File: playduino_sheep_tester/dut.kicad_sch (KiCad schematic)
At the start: 48 parts, among them J2 Conn_02x14_Odd_Even, J3 Conn_01x04_Pin, K2 G6K-2F-Y-TR DC5, K3 G6K-2F-Y-TR DC5, K4 G6K-2F-Y-TR DC5, K5 G6K-2F-Y-TR DC5, K6 G6K-2F-Y-TR DC5, Q11 AO3416, Q12 AO3416, Q13 AO3416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

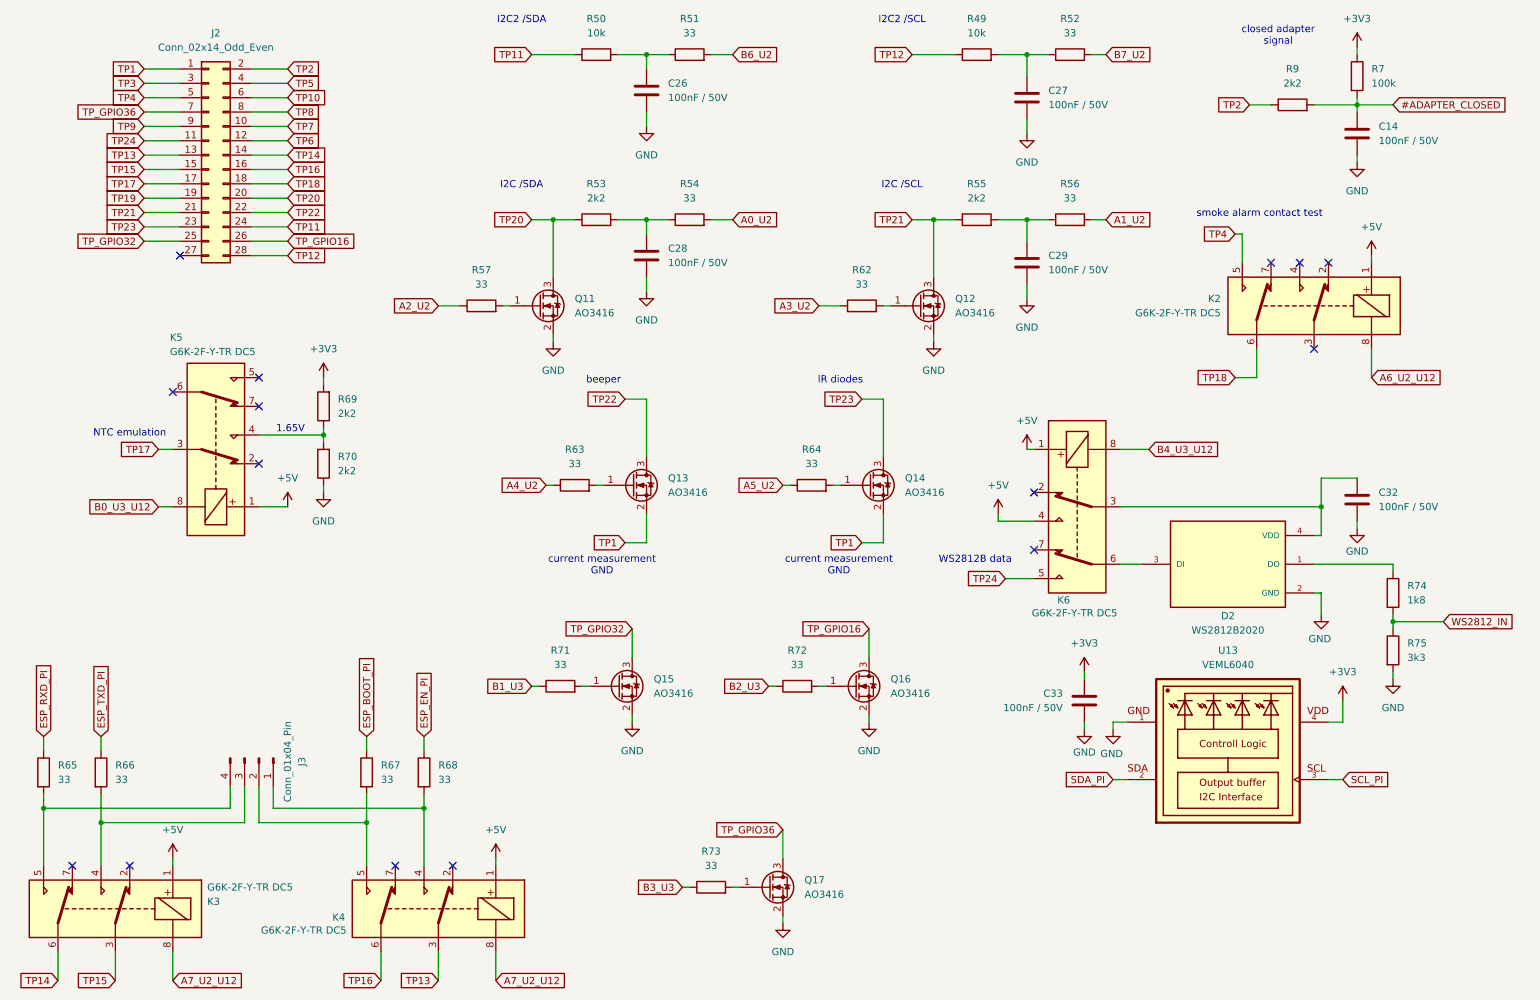
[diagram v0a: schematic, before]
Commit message: small improvements and fixing horrible mistakes
change A3_U2 and B7_U2 because of known issues with MCP23017
https://support.microchip.com/s/article/GPA7---GPB7-Cannot-Be-Used-as-Inputs-In-MCP23017

add resistor to MCP23017 address pins

replace B3_U2 duplicate with B6_U3
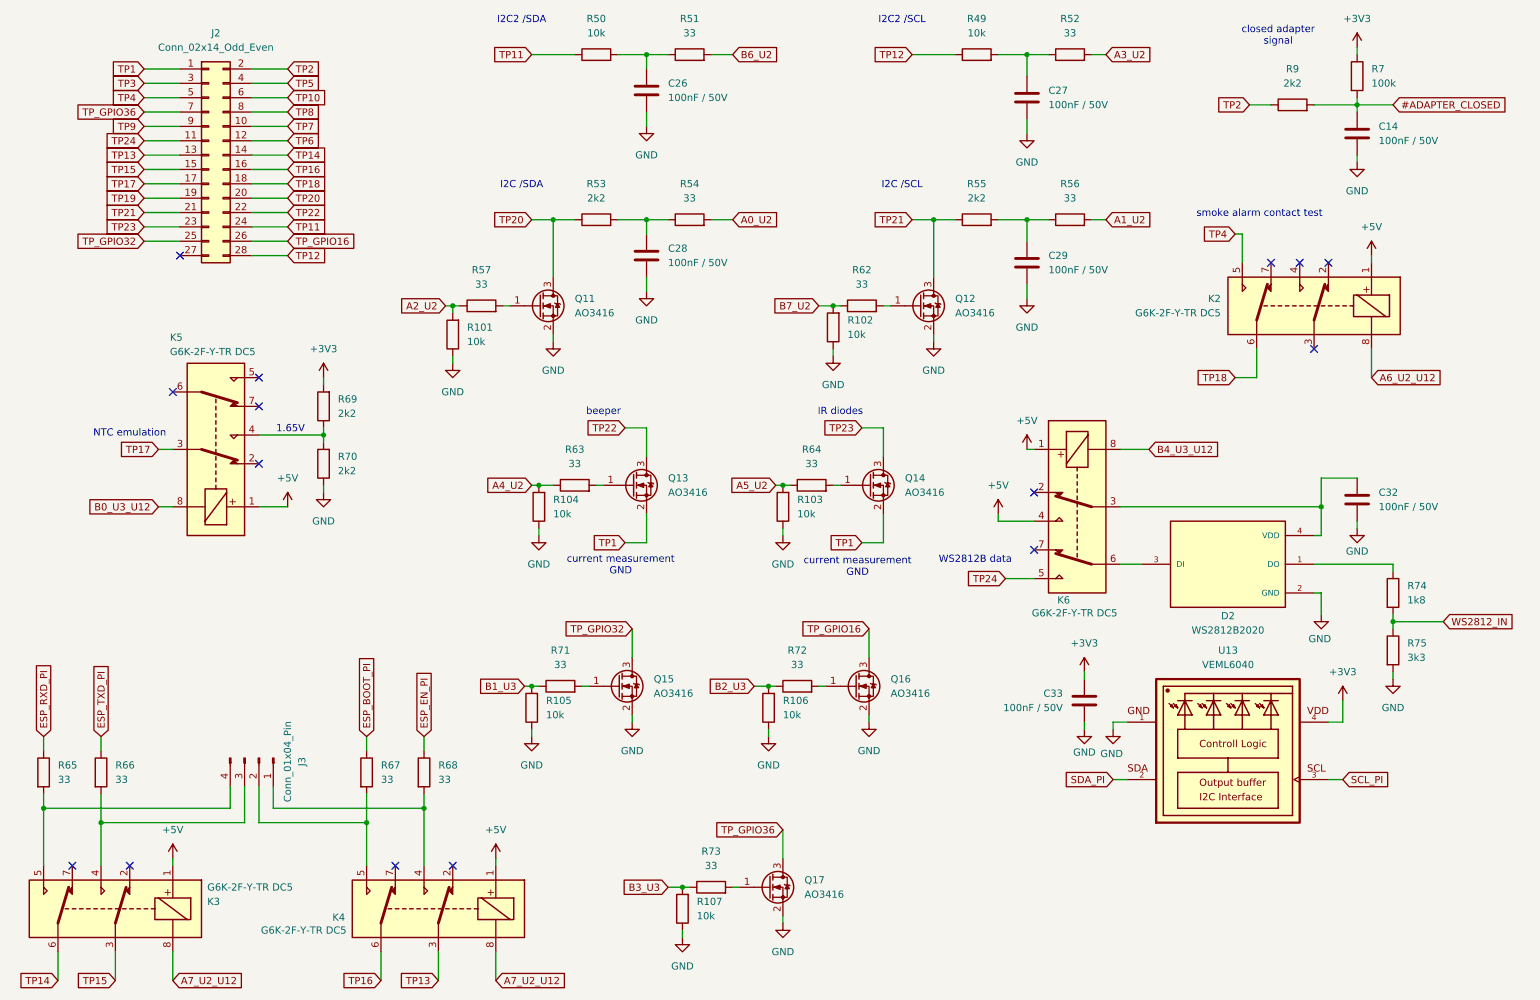
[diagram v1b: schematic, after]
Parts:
- added R101, R102, R103, R104, R105, R106, R107: 10k, Resistor_SMD:R_0603_1608Metric, symbol Device:R
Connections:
- net A2_U2: now also R101.2
- net A3_U2: now also R52.2; no longer R62.1
- net A4_U2: now also R104.2
- net A5_U2: now also R103.2
- net B1_U3: now also R105.2
- net B2_U3: now also R106.2
- net B3_U3: now also R107.2
- net B7_U2: now also R62.1, R102.2; no longer R52.2
- net GND: now also R101.1, R102.1, R103.1, R104.1, R105.1, R106.1, R107.1

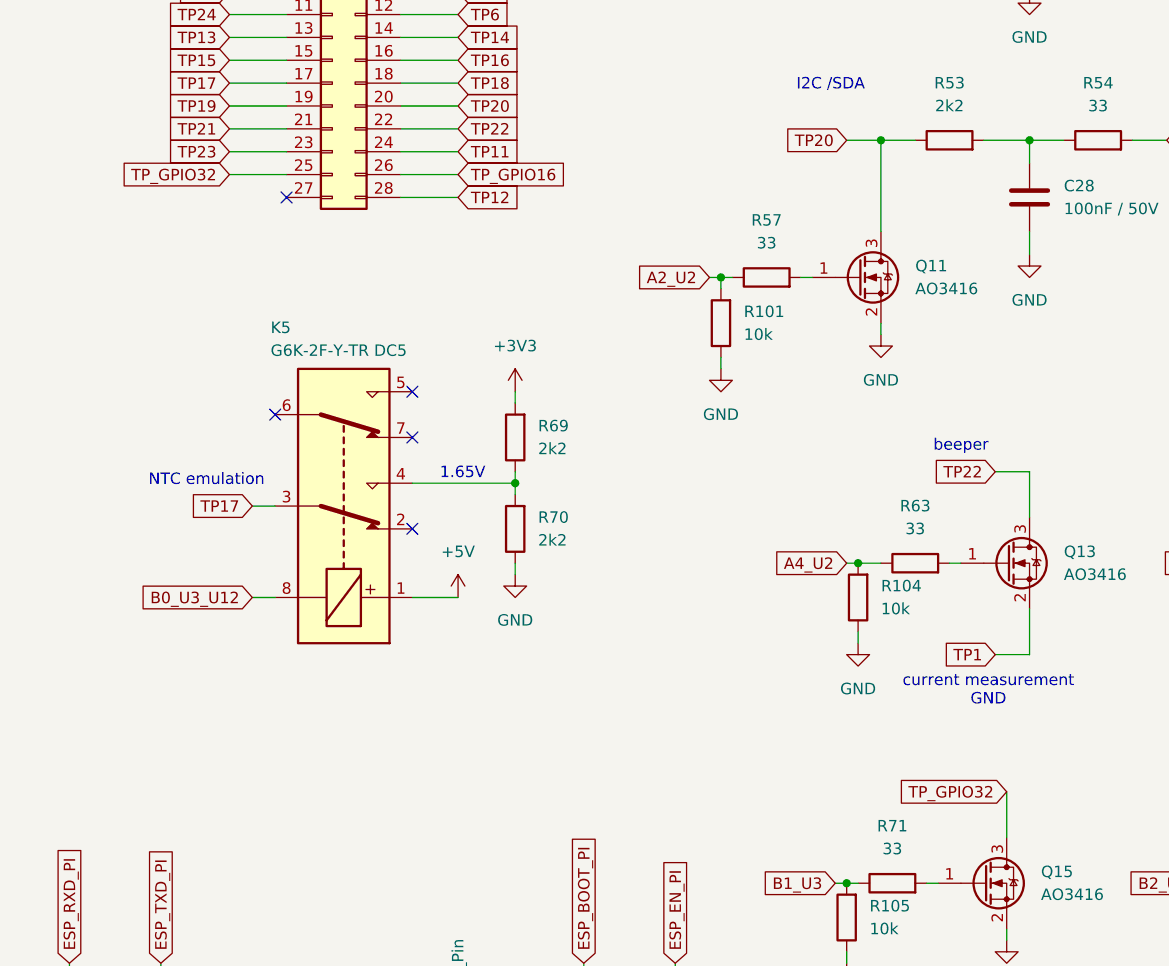
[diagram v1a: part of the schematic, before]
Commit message: correct GPIO35 for PaPir Testpoint
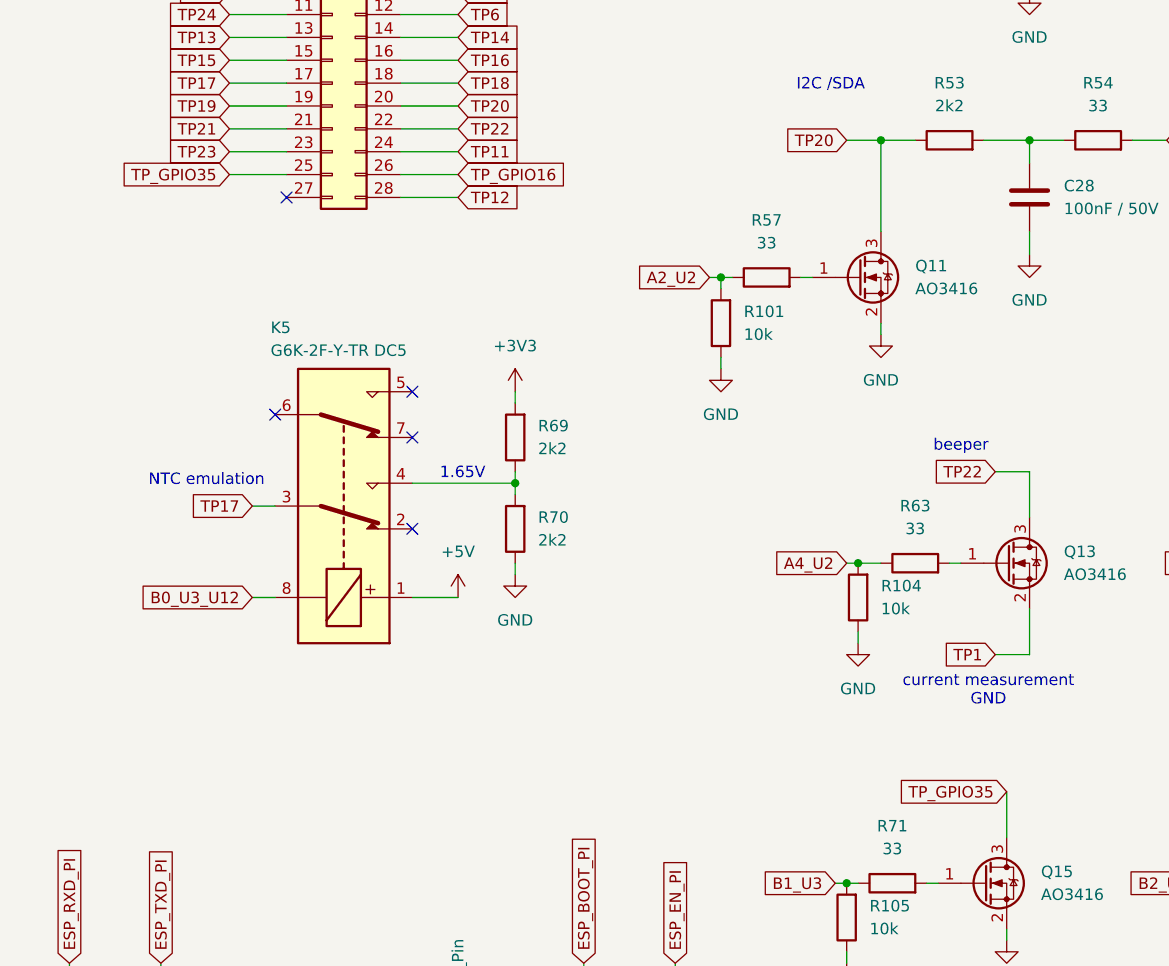
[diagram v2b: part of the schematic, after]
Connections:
- net TP_GPIO32 renamed TP_GPIO35
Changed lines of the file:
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@@
 		)
 	)
-	(global_label "TP_GPIO32"
+	(global_label "TP_GPIO35"
 		(shape input)
 		(at 40.64 58.42 180)
@@
 		)
 	)
-	(global_label "TP_GPIO32"
+	(global_label "TP_GPIO35"
 		(shape input)
 		(at 127 127 180)
